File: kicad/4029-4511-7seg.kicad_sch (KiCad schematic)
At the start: 14 parts, among them U13 4029, U14 4511, U15 TDSR-3163-G

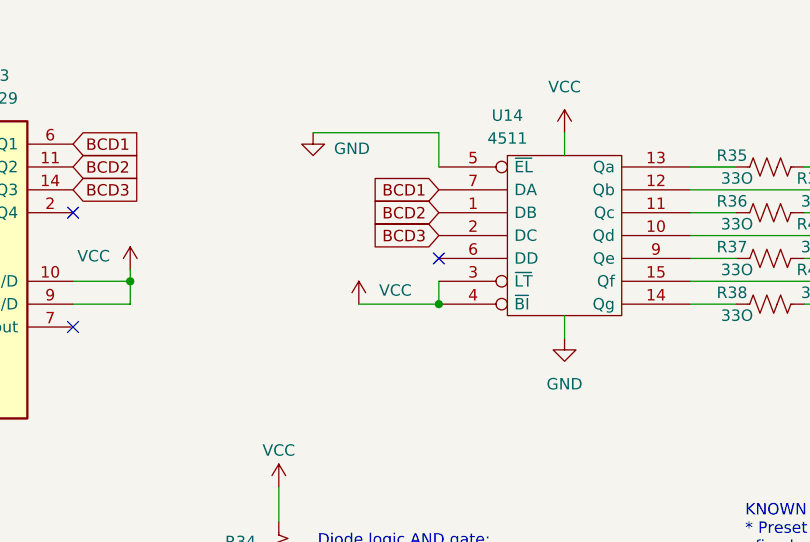
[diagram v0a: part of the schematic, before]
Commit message: Fix missing 4511 BCD pin
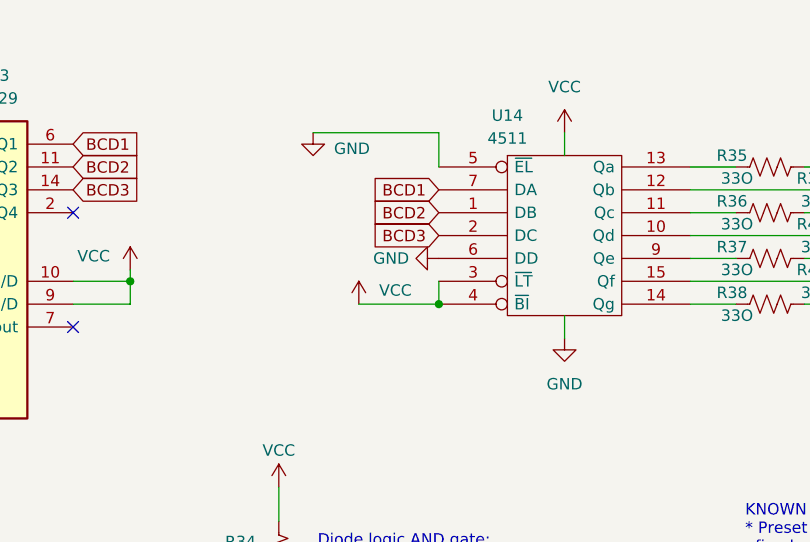
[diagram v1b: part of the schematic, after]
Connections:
- net GND: now also U14.6 (DD)
- no-connect marks 4 -> 3
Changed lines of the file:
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@@
-	)
-	(no_connect
-		(at 165.1 95.25)
 	)
 	(no_connect
@@
 					(unit 1)
 				)
+			)
+		)
+	)
+	(symbol
+		(lib_name "GND_1")
+		(lib_id "power:GND")
+		(at 165.1 95.25 270)
+		(unit 1)
+		(exclude_from_sim no)
+		(in_bom yes)
+		(on_board yes)
+		(dnp no)
+		(property "Reference" "#PWR065"
+			(at 158.75 95.25 0)
+			(effects
+				(font
+					(size 1.27 1.27)
+				)
+				(hide yes)
+			)
+		)
+		(property "Value" "GND"
+			(at 161.798 95.25 90)
+			(effects
+				(font
+					(size 1.27 1.27)
+				)
+				(justify right)
+			)
+		)
+		(property "Footprint" ""
+			(at 165.1 95.25 0)
+			(effects
+				(font
+					(size 1.27 1.27)
+				)
+				(hide yes)
+			)
+		)
+		(property "Datasheet" ""
+			(at 165.1 95.25 0)
+			(effects
+				(font
+					(size 1.27 1.27)
+				)
+				(hide yes)
+			)
+		)
+		(property "Description" "Power symbol creates a global label with name \"GND\" , ground"
+			(at 165.1 95.25 0)
+			(effects
+				(font
+					(size 1.27 1.27)
+				)
+				(hide yes)
+			)
+		)
+		(pin "1"
+		)
+		(instances
+			(project "space_dice"
+				(path "/bcd0d850-a20d-42e1-b97f-b14f9222717c/87c438b6-db97-4b05-b602-e587fa01b059"
+					(reference "#PWR065")
+					(unit 1)
+				)
